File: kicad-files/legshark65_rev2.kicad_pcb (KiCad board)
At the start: 2 copper layers, 281 x 93.9 mm, 183 parts, among them J1 ARM JTAG, J2 Conn_01x04, SW1 K2-1187SQ-A4SW-06, SW2 PCM12SMTR, T2 53261-0471, U1 STM32F411CEU6, U3 AT24C256C-SSHL-T, Y1 TAXM8M4RFDCET2T

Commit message: Started routing the switches
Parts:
- moved D_15 12.2 mm to (22.0, 32.6), turned to 90 degrees
- moved D_45 12.2 mm to (22.0, 70.7), turned to 90 degrees
- moved D_29 11.4 mm to (279.4, 32.6), turned to 90 degrees
- moved D_59 11.4 mm to (279.4, 70.7), turned to 90 degrees
- moved D_44 11.4 mm to (279.3, 51.7), turned to 90 degrees
- moved D_61 11.0 mm to (64.5, 79.2)
- moved D_23 10.6 mm to (170.3, 32.6), turned to 90 degrees
- moved D_25 10.6 mm to (208.4, 32.6), turned to 90 degrees
- moved D_28 10.6 mm to (265.6, 32.6), turned to 90 degrees
- moved D_38 10.6 mm to (170.3, 51.7), turned to 90 degrees
- moved D_40 10.6 mm to (208.4, 51.7), turned to 90 degrees
- moved D_43 10.6 mm to (265.6, 51.7), turned to 90 degrees
- moved D_53 10.6 mm to (170.3, 70.7), turned to 90 degrees
- moved D_55 10.6 mm to (208.4, 70.7), turned to 90 degrees
- moved D_58 10.6 mm to (265.6, 70.7), turned to 90 degrees
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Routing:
- net row2: track 0.00 -> 261.4 mm
- net row0: track 0.00 -> 261.3 mm
- net row3: track 0.00 -> 257.4 mm
- net row1: track 0.00 -> 257.3 mm
- net col8: track 0.00 -> 86.8 mm
- net col2: track 0.00 -> 85.7 mm
- net col6: track 0.00 -> 85.5 mm
- net col1: track 0.00 -> 82.7 mm
- net col4: track 0.00 -> 82.7 mm
- net col7: track 0.00 -> 76.1 mm
- net col3: track 0.00 -> 76.1 mm
- net col14: track 0.00 -> 66.9 mm
- net col5: track 0.00 -> 56.9 mm
- net col0: track 0.00 -> 40.1 mm
- net Net-(D_44-A): track 0.00 -> 18.1 mm
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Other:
- board size 281 x 93.9 mm -> 285.8 x 93.9 mm

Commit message: Added ground fill
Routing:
- added copper zone on B.Cu, net GND
- added copper zone on F.Cu, net GND
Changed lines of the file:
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@@
     (pad_to_mask_clearance 0)
     (aux_axis_origin 9.525 9.525)
+    (grid_origin 9.525 9.525)
     (pcbplotparams
       (layerselection 0x00010fc_ffffffff)
@@
   (segment (start 116.84 80.645) (end 126.365 80.645) (width 0.5) (layer "B.Cu") (net 92))
   (segment (start 164.465 80.645) (end 173.99 80.645) (width 0.5) (layer "B.Cu") (net 93))
+  (zone (net 22) (net_name "GND") (layers "F&B.Cu") (hatch edge 0.5)
+    (connect_pads (clearance 0.508))
+    (min_thickness 0.25) (filled_areas_thickness no)
+    (fill (thermal_gap 0.5) (thermal_bridge_width 0.5))
+    (polygon
+      (pts
+        (xy -2.38125 -2.38125)
+        (xy 288.13125 -2.38125)
+        (xy 288.13125 97.63125)
+        (xy -2.38125 97.63125)
+      )
+    )
+  )
   (group "" (id 11be46ce-dac0-4760-b84c-234ba0bcab25)
     (members

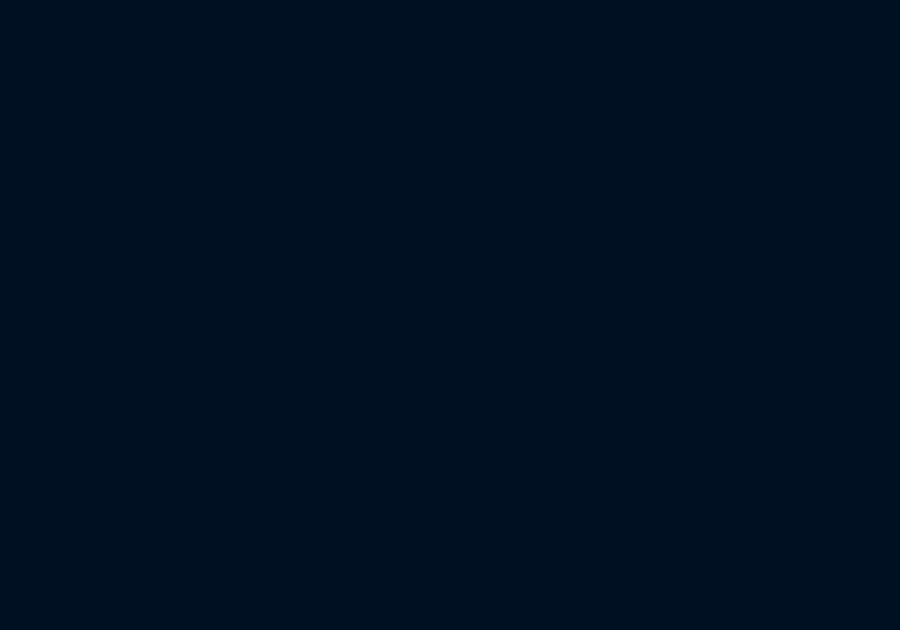
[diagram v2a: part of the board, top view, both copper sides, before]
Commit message: Added the 5V to 3V3 stepdown schematic from db to the mb
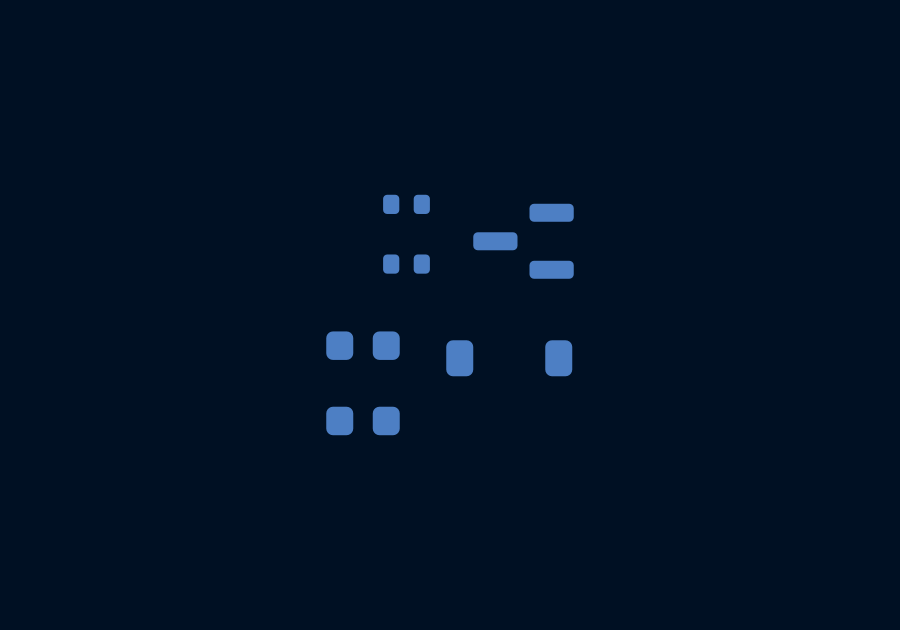
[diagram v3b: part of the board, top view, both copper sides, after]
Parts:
- added C3: 1uF, Capacitor_SMD:C_0603_1608Metric, B.Cu at (310.0, 73.7)
- added C5: 1uF, Capacitor_SMD:C_0603_1608Metric, B.Cu at (310.0, 76.2)
- added D1: B5819W-SL, Diode_SMD:D_SOD-123, B.Cu at (314.9, 74.1)
- added R4: 100k, Resistor_SMD:R_0402_1005Metric, B.Cu at (311.4, 69.0)
- added R9: 100k, Resistor_SMD:R_0402_1005Metric, B.Cu at (311.4, 71.0)
- added U2: MCP1700T-3302E/TT, Package_TO_SOT_SMD:SOT-23, B.Cu at (315.3, 70.2)
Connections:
- J2 pad 4: 3V3 -> 5V
- T2 pad 1: 3V3 -> 5V

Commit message: Made more connections
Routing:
- net Net-(D_0-A): track 0.00 -> 11.0 mm
- net Net-(D_58-A): track 0.00 -> 10.6 mm
- net Net-(D_51-A): track 0.00 -> 10.6 mm
- net Net-(D_57-A): track 0.00 -> 10.6 mm
- net Net-(D_55-A): track 0.00 -> 10.6 mm
- net Net-(D_54-A): track 0.00 -> 10.6 mm
- net Net-(D_53-A): track 0.00 -> 10.6 mm
- net Net-(D_52-A): track 0.00 -> 10.6 mm
- net Net-(D_50-A): track 0.00 -> 10.6 mm
- net Net-(D_56-A): track 0.00 -> 10.6 mm
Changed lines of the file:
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@@
       )
       (stroke (width 0) (type solid)) (fill solid) (layer "F.Mask"))
-    (group "" (id b3d5d112-ef3e-422d-ae13-66f38a1f1e1a)
+    (group "" (id 66c91c08-0ac4-4b9b-bb75-66e34729ec92)
       (members
-        49a57371-b691-4317-9c23-1251913fd7ea
-        d1a6b762-c5dc-4ab4-8a80-884b8537de66
+        06b6816c-cec1-4f6e-bc3f-2c0de491363b
+        3c2629a1-1c4a-4caf-9ee5-35ed36f8af8b
       )
     )
-    (group "" (id 3babff80-47ff-4ec6-b978-37f08f1585c6)
+    (group "" (id d62d97a6-698a-486e-b5b1-5f49cb15a870)
       (members
-        667760dc-c4c3-44dd-9f2a-b68ffec0febf
-        ce826385-a9c0-48b1-9f68-7a1952938f2f
+        1b36dae7-a4fb-4e4a-af06-6056aa50aacb
+        84a61f4d-a16a-4f9d-a61a-97b50aaa47cd
       )
     )
@@
   (segment (start 22.025 71.425) (end 279.349109 71.425) (width 0.5) (layer "B.Cu") (net 19))
   (arc (start 279.349109 71.425) (mid 279.383919 71.418076) (end 279.41343 71.398357) (width 0.5) (layer "B.Cu") (net 19))
+  (segment (start 15.880721 8.260721) (end 12.065 4.445) (width 0.25) (layer "B.Cu") (net 28))
+  (arc (start 17.981162 13.331634) (mid 17.435275 10.587276) (end 15.880721 8.260721) (width 0.25) (layer "B.Cu") (net 28))
   (segment (start 34.924893 8.254893) (end 31.115 4.445) (width 0.25) (layer "B.Cu") (net 29))
   (arc (start 37.025 13.325) (mid 36.4792 10.581078) (end 34.924893 8.254893) (width 0.25) (layer "B.Cu") (net 29))
@@
   (segment (start 92.318369 65.64837) (end 88.265 61.595) (width 0.25) (layer "B.Cu") (net 77))
   (arc (start 94.133007 70.029292) (mid 93.661398 67.658354) (end 92.318369 65.64837) (width 0.25) (layer "B.Cu") (net 77))
+  (segment (start 111.368369 65.64837) (end 107.315 61.595) (width 0.25) (layer "B.Cu") (net 78))
+  (arc (start 113.183007 70.029292) (mid 112.711398 67.658354) (end 111.368369 65.64837) (width 0.25) (layer "B.Cu") (net 78))
+  (segment (start 130.418369 65.64837) (end 126.365 61.595) (width 0.25) (layer "B.Cu") (net 79))
+  (arc (start 132.233007 70.029292) (mid 131.761398 67.658354) (end 130.418369 65.64837) (width 0.25) (layer "B.Cu") (net 79))
+  (segment (start 149.468369 65.64837) (end 145.415 61.595) (width 0.25) (layer "B.Cu") (net 80))
+  (arc (start 151.283007 70.029292) (mid 150.811398 67.658354) (end 149.468369 65.64837) (width 0.25) (layer "B.Cu") (net 80))
+  (segment (start 168.518369 65.64837) (end 164.465 61.595) (width 0.25) (layer "B.Cu") (net 81))
+  (arc (start 170.333007 70.029292) (mid 169.861398 67.658354) (end 168.518369 65.64837) (width 0.25) (layer "B.Cu") (net 81))
+  (segment (start 187.568369 65.64837) (end 183.515 61.595) (width 0.25) (layer "B.Cu") (net 82))
+  (arc (start 189.383007 70.029292) (mid 188.911398 67.658354) (end 187.568369 65.64837) (width 0.25) (layer "B.Cu") (net 82))
+  (segment (start 206.618369 65.64837) (end 202.565 61.595) (width 0.25) (layer "B.Cu") (net 83))
+  (arc (start 208.433007 70.029292) (mid 207.961398 67.658354) (end 206.618369 65.64837) (width 0.25) (layer "B.Cu") (net 83))
+  (segment (start 225.668369 65.64837) (end 221.615 61.595) (width 0.25) (layer "B.Cu") (net 84))
+  (arc (start 227.483007 70.029292) (mid 227.011398 67.658354) (end 225.668369 65.64837) (width 0.25) (layer "B.Cu") (net 84))
+  (segment (start 244.718369 65.64837) (end 240.665 61.595) (width 0.25) (layer "B.Cu") (net 85))
+  (arc (start 246.533007 70.029292) (mid 246.061398 67.658354) (end 244.718369 65.64837) (width 0.25) (layer "B.Cu") (net 85))
+  (segment (start 263.768369 65.64837) (end 259.715 61.595) (width 0.25) (layer "B.Cu") (net 86))
+  (arc (start 265.583007 70.029292) (mid 265.111398 67.658354) (end 263.768369 65.64837) (width 0.25) (layer "B.Cu") (net 86))
   (segment (start 279.41343 69.998357) (end 279.41343 63.160448) (width 0.25) (layer "B.Cu") (net 87))
   (arc (start 279.41343 63.160448) (mid 279.244909 62.313234) (end 278.765 61.595) (width 0.25) (layer "B.Cu") (net 87))

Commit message: More routing
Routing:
- net col13: track 0.00 -> 79.5 mm
- net col11: track 0.00 -> 76.1 mm
- net col12: track 0.00 -> 76.1 mm
- net col10: track 0.00 -> 76.1 mm
- net col9: track 0.00 -> 57.1 mm
- net col0: track 40.1 -> 80.1 mm
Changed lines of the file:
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@@
   (gr_line (start 139.507392 92.868763) (end 129.573869 92.868748)
     (stroke (width 0.1) (type default)) (layer "Edge.Cuts"))
-  (segment (start 5.715 64.135) (end 4.411223 62.831223) (width 0.5) (layer "F.Cu") (net 1))
+  (segment (start 6.425 53.007514) (end 6.425 46.799091) (width 0.5) (layer "F.Cu") (net 1))
+  (segment (start 6.325 14.19363) (end 6.325 8.45767) (width 0.5) (layer "F.Cu") (net 1))
+  (segment (start 5.339214 16.310787) (end 5.525 16.125) (width 0.5) (layer "F.Cu") (net 1))
+  (segment (start 5.425 32.325) (end 4.905372 32.844628) (width 0.5) (layer "F.Cu") (net 1))
   (segment (start 5.715 26.035) (end 15.24 26.035) (width 0.5) (layer "F.Cu") (net 1))
+  (segment (start 5.325 55.525) (end 5.422685 55.427315) (width 0.5) (layer "F.Cu") (net 1))
+  (segment (start 6.425 29.910902) (end 6.425 27.749091) (width 0.5) (layer "F.Cu") (net 1))
   (segment (start 5.715 64.135) (end 15.24 64.135) (width 0.5) (layer "F.Cu") (net 1))
-  (segment (start 6.525 50.643613) (end 6.525 47.040512) (width 0.5) (layer "F.Cu") (net 1))
-  (segment (start 5.901765 52.148235) (end 4.212098 53.837902) (width 0.5) (layer "F.Cu") (net 1))
-  (segment (start 3.525 60.691692) (end 3.525 55.496703) (width 0.5) (layer "F.Cu") (net 1))
-  (arc (start 3.525 55.496703) (mid 3.703571 54.598966) (end 4.212098 53.837902) (width 0.5) (layer "F.Cu") (net 1))
-  (arc (start 4.411223 62.831223) (mid 3.755322 61.849598) (end 3.525 60.691692) (width 0.5) (layer "F.Cu") (net 1))
-  (arc (start 5.901765 52.148235) (mid 6.363026 51.457909) (end 6.525 50.643613) (width 0.5) (layer "F.Cu") (net 1))
-  (arc (start 6.525 47.040512) (mid 6.314488 45.982197) (end 5.715 45.085) (width 0.5) (layer "F.Cu") (net 1))
+  (segment (start 3.925 40.763558) (end 3.925 35.211455) (width 0.5) (layer "F.Cu") (net 1))
+  (segment (start 4.025 60.819557) (end 4.025 58.663477) (width 0.5) (layer "F.Cu") (net 1))
+  (segment (start 3.925 21.713558) (end 3.925 19.725) (width 0.5) (layer "F.Cu") (net 1))
+  (segment (start 5.715 64.135) (end 5.174363 63.594363) (width 0.5) (layer "F.Cu") (net 1))
+  (arc (start 5.422685 55.427315) (mid 6.164506 54.317101) (end 6.425 53.007514) (width 0.5) (layer "F.Cu") (net 1))
+  (arc (start 4.025 58.663477) (mid 4.362859 56.964946) (end 5.325 55.525) (width 0.5) (layer "F.Cu") (net 1))
+  (arc (start 5.425 32.325) (mid 6.165118 31.217385) (end 6.425 29.910902) (width 0.5) (layer "F.Cu") (net 1))
+  (arc (start 5.525 16.125) (mid 6.117087 15.238881) (end 6.325 14.19363) (width 0.5) (layer "F.Cu") (net 1))
+  (arc (start 5.174363 63.594363) (mid 4.32371 62.321271) (end 4.025 60.819557) (width 0.5) (layer "F.Cu") (net 1))
+  (arc (start 6.425 27.749091) (mid 6.240478 26.821432) (end 5.715 26.035) (width 0.5) (layer "F.Cu") (net 1))
+  (arc (start 5.715 26.035) (mid 4.390206 24.052306) (end 3.925 21.713558) (width 0.5) (layer "F.Cu") (net 1))
+  (arc (start 3.925 19.725) (mid 4.292542 17.877241) (end 5.339214 16.310787) (width 0.5) (layer "F.Cu") (net 1))
+  (arc (start 6.325 8.45767) (mid 6.166466 7.660667) (end 5.715 6.985) (width 0.5) (layer "F.Cu") (net 1))
+  (arc (start 5.715 45.085) (mid 4.390206 43.102306) (end 3.925 40.763558) (width 0.5) (layer "F.Cu") (net 1))
+  (arc (start 6.425 46.799091) (mid 6.240478 45.871432) (end 5.715 45.085) (width 0.5) (layer "F.Cu") (net 1))
+  (arc (start 3.925 35.211455) (mid 4.17979 33.930537) (end 4.905372 32.844628) (width 0.5) (layer "F.Cu") (net 1))
   (segment (start 24.87 45.19) (end 24.765 45.085) (width 0.5) (layer "F.Cu") (net 2))
   (segment (start 24.765 26.035) (end 24.87 25.93) (width 0.5) (layer "F.Cu") (net 2))
   (segment (start 24.87 25.93) (end 24.87 7.09) (width 0.5) (layer "F.Cu") (net 2))
   (segment (start 24.765 64.135) (end 25.254099 64.624099) (width 0.5) (layer "F.Cu") (net 2))
+  (segment (start 25.695553 43.174524) (end 25.695553 27.7941) (width 0.5) (layer "F.Cu") (net 2))
   (segment (start 25.525 81.350198) (end 25.525 65.969802) (width 0.5) (layer "F.Cu") (net 2))
   (segment (start 24.87 64.03) (end 24.87 45.19) (width 0.5) (layer "F.Cu") (net 2))
-  (segment (start 26.025 42.043091) (end 26.025 29.076909) (width 0.5) (layer "F.Cu") (net 2))
   (segment (start 24.765 83.185) (end 29.5275 83.185) (width 0.5) (layer "F.Cu") (net 2))
   (segment (start 24.765 64.135) (end 24.87 64.03) (width 0.5) (layer "F.Cu") (net 2))
   (arc (start 25.525 65.969802) (mid 25.327483 64.976815) (end 24.765 64.135) (width 0.5) (layer "F.Cu") (net 2))
   (arc (start 24.765 83.185) (mid 25.327483 82.343186) (end 25.525 81.350198) (width 0.5) (layer "F.Cu") (net 2))
-  (arc (start 24.765 45.085) (mid 25.697537 43.689361) (end 26.025 42.043091) (width 0.5) (layer "F.Cu") (net 2))
-  (arc (start 26.025 29.076909) (mid 25.697537 27.43064) (end 24.765 26.035) (width 0.5) (layer "F.Cu") (net 2))
+  (arc (start 25.695553 27.7941) (mid 25.498036 26.801113) (end 24.935553 25.959298) (width 0.5) (layer "F.Cu") (net 2))
+  (arc (start 24.935553 45.009298) (mid 25.498035 44.1675) (end 25.695553 43.174524) (width 0.5) (layer "F.Cu") (net 2))
   (segment (start 43.92 83.08) (end 43.92 7.09) (width 0.5) (layer "F.Cu") (net 3))
   (segment (start 43.815 83.185) (end 43.92 83.08) (width 0.5) (layer "F.Cu") (net 3))
@@
   (arc (start 156.52498 72.357029) (mid 156.677864 71.588347) (end 157.113289 70.936696) (width 0.5) (layer "F.Cu") (net 9))
   (arc (start 158.525 65.124827) (mid 158.418445 64.589136) (end 158.115 64.135) (width 0.5) (layer "F.Cu") (net 9))
+  (segment (start 177.165 64.135) (end 177.27 64.03) (width 0.5) (layer "F.Cu") (net 10))
+  (segment (start 177.27 64.03) (end 177.27 7.09) (width 0.5) (layer "F.Cu") (net 10))
+  (segment (start 196.32 83.08) (end 196.32 7.09) (width 0.5) (layer "F.Cu") (net 11))
+  (segment (start 196.215 83.185) (end 196.32 83.08) (width 0.5) (layer "F.Cu") (net 11))
+  (segment (start 215.265 83.185) (end 215.37 83.08) (width 0.5) (layer "F.Cu") (net 12))
+  (segment (start 215.37 83.08) (end 215.37 7.09) (width 0.5) (layer "F.Cu") (net 12))
+  (segment (start 234.42 83.08) (end 234.42 7.09) (width 0.5) (layer "F.Cu") (net 13))
+  (segment (start 234.315 83.185) (end 234.42 83.08) (width 0.5) (layer "F.Cu") (net 13))
+  (segment (start 253.365 83.185) (end 253.47 83.08) (width 0.5) (layer "F.Cu") (net 14))
+  (segment (start 253.365 45.085) (end 252.146915 43.866915) (width 0.5) (layer "F.Cu") (net 14))
+  (segment (start 253.365 26.035) (end 253.47 25.93) (width 0.5) (layer "F.Cu") (net 14))
+  (segment (start 251.988459 36.361541) (end 253.239435 35.110565) (width 0.5) (layer "F.Cu") (net 14))
+  (segment (start 253.925 49.917116) (end 253.925 46.436959) (width 0.5) (layer "F.Cu") (net 14))
+  (segment (start 253.47 25.93) (end 253.47 7.09) (width 0.5) (layer "F.Cu") (net 14))
+  (segment (start 253.47 83.08) (end 253.47 64.24) (width 0.5) (layer "F.Cu") (net 14))
+  (segment (start 252.127414 52.922586) (end 253.070897 51.979103) (width 0.5) (layer "F.Cu") (net 14))
+  (segment (start 253.925 33.455464) (end 253.925 27.386959) (width 0.5) (layer "F.Cu") (net 14))
+  (segment (start 253.47 64.24) (end 253.365 64.135) (width 0.5) (layer "F.Cu") (net 14))
+  (segment (start 253.365 64.135) (end 251.993596 62.763596) (width 0.5) (layer "F.Cu") (net 14))
+  (segment (start 251.425 42.124058) (end 251.425 37.721851) (width 0.5) (layer "F.Cu") (net 14))
+  (segment (start 251.425 61.390884) (end 251.425 54.618365) (width 0.5) (layer "F.Cu") (net 14))
+  (arc (start 253.239435 35.110565) (mid 253.746828 34.351198) (end 253.925 33.455464) (width 0.5) (layer "F.Cu") (net 14))
+  (arc (start 251.993596 62.763596) (mid 251.572773 62.13379) (end 251.425 61.390884) (width 0.5) (layer "F.Cu") (net 14))
+  (arc (start 253.925 46.436959) (mid 253.779461 45.705285) (end 253.365 45.085) (width 0.5) (layer "F.Cu") (net 14))
+  (arc (start 253.925 27.386959) (mid 253.779461 26.655285) (end 253.365 26.035) (width 0.5) (layer "F.Cu") (net 14))
+  (arc (start 251.425 54.618365) (mid 251.607552 53.700616) (end 252.127414 52.922586) (width 0.5) (layer "F.Cu") (net 14))
+  (arc (start 253.070897 51.979103) (mid 253.703026 51.033055) (end 253.925 49.917116) (width 0.5) (layer "F.Cu") (net 14))
+  (arc (start 252.146915 43.866915) (mid 251.61262 43.067285) (end 251.425 42.124058) (width 0.5) (layer "F.Cu") (net 14))
+  (arc (start 251.425 37.721851) (mid 251.571438 36.985656) (end 251.988459 36.361541) (width 0.5) (layer "F.Cu") (net 14))
   (segment (start 272.52 44.98) (end 272.52 26.14) (width 0.5) (layer "F.Cu") (net 15))
   (segment (start 262.89 45.085) (end 272.415 45.085) (width 0.5) (layer "F.Cu") (net 15))

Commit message: Ripped up traces and started placing io
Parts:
- added D_71: D, Diode_SMD:D_SOD-523, B.Cu at (111.9, 79.3)
- added D_72: D, Diode_SMD:D_SOD-523, B.Cu at (188.1, 79.3)
- added K_71: KEYSW, MX_Only:MXOnly-1U-NoLED, F.Cu at (104.8, 85.7)
- added K_73: KEYSW, MX_Only:MXOnly-1U-NoLED, F.Cu at (181.0, 85.7)
- moved C16 201.7 mm to (121.4, 112.9), turned to 90 degrees
- moved U1 196.2 mm to (152.4, 57.1), turned to 90 degrees
- moved R11 195.1 mm to (163.5, 114.2)
- moved R15 195.1 mm to (163.5, 116.7)
- moved SW1 193.6 mm to (154.1, 122.0)
- moved C7 192.8 mm to (153.9, 109.5)
- moved C17 192.8 mm to (145.2, 109.5)
- moved R7 185.9 mm to (159.5, 52.4)
- moved C1 184.9 mm to (152.4, 69.1), turned to 0 degrees
- moved C2 184.8 mm to (152.4, 71.4)
- moved SW2 181.6 mm to (154.8, 114.3)
- moved R8 178.5 mm to (166.7, 50.0)
- moved C6 169.9 mm to (164.3, 52.4)
- moved Y1 167.7 mm to (152.4, 65.4)
- moved J1 151.6 mm to (208.3, 114.3)
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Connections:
- T2 pad 1: 5V -> GND
- T2 pad 2: D- -> D+
- T2 pad 3: D+ -> D-
- T2 pad 4: GND -> 5V
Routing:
- net row2: track 261.4 -> 0.00 mm
- net row0: track 261.3 -> 0.00 mm
- net row3: track 257.4 -> 0.00 mm
- net row1: track 257.3 -> 0.00 mm
- net col8: track 86.8 -> 0.00 mm
- net col2: track 85.7 -> 0.00 mm
- net col6: track 85.5 -> 0.00 mm
- net col4: track 82.7 -> 0.00 mm
- net col1: track 82.4 -> 0.00 mm
- net col0: track 80.1 -> 0.00 mm
- net col13: track 79.5 -> 0.00 mm
- net col11: track 76.1 -> 0.00 mm
- net col7: track 76.1 -> 0.00 mm
- net col12: track 76.1 -> 0.00 mm
- net col10: track 76.1 -> 0.00 mm
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
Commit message: Updated layout in readme
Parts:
- moved R7 37.4 mm to (196.8, 54.8)
- moved C6 32.9 mm to (196.8, 57.1)
- moved R8 31.6 mm to (196.8, 59.5)
- moved D_65 24.4 mm to (154.8, 88.1), turned to 90 degrees
- moved U3 23.8 mm to (190.5, 57.1)
- moved D_15 19.7 mm to (2.38, 31.0)
- moved D_45 19.7 mm to (2.38, 69.1)
- moved D_71 16.8 mm to (97.6, 88.1), turned to 90 degrees
- moved D_43 15.6 mm to (250.0, 50.0)
- moved D_69 8.96 mm to (264.3, 88.1), turned to 90 degrees
- moved D_70 8.96 mm to (150.0, 88.1), turned to 90 degrees
- moved D_64 8.95 mm to (131.0, 88.1), turned to 90 degrees
- moved D_68 8.95 mm to (245.3, 88.1), turned to 90 degrees
- moved D_67 8.95 mm to (226.2, 88.1), turned to 90 degrees
- moved D_60 8.93 mm to (40.5, 88.1), turned to 90 degrees
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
